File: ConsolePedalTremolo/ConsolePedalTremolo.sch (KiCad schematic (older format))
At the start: 30 parts, among them J1 Conn_02x25_Counter_Clockwise, Q1 BC550, Q2 BC550, Q3 BC550

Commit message: Assigned footprints. Need to add another resistor since the only ptv09 potentiometers I could find only went up to 500k
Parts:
- C1, C2, C3, C4, C6, C7: footprint (none) -> Capacitor_THT:C_Axial_L12.0mm_D6.5mm_P20.00mm_Horizontal
- C5: footprint (none) -> Capacitor_THT:CP_Axial_L11.0mm_D6.0mm_P18.00mm_Horizontal
- R1, R10, R11, R12, R13, R2, R4, R5, R6, R7, R8, R9: footprint (none) -> Resistor_THT:R_Axial_DIN0207_L6.3mm_D2.5mm_P10.16mm_Horizontal
- RV1, RV2: footprint (none) -> Potentiometer_THT:Potentiometer_Bourns_PTV09A-1_Single_Vertical
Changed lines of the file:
@@
 F 0 "R1" H 3020 2896 50  0000 L CNN
 F 1 "1M" H 3020 2805 50  0000 L CNN
-F 2 "" V 2880 2850 50  0001 C CNN
+F 2 "Resistor_THT:R_Axial_DIN0207_L6.3mm_D2.5mm_P10.16mm_Horizontal" V 2880 2850 50  0001 C CNN
 F 3 "~" H 2950 2850 50  0001 C CNN
 	1    2950 2850
@@
 F 0 "C1" V 3048 2700 50  0000 C CNN
 F 1 "0.1uF" V 3139 2700 50  0000 C CNN
-F 2 "" H 3338 2550 50  0001 C CNN
+F 2 "Capacitor_THT:C_Axial_L12.0mm_D6.5mm_P20.00mm_Horizontal" H 3338 2550 50  0001 C CNN
 F 3 "~" H 3300 2700 50  0001 C CNN
 	1    3300 2700
@@
 F 0 "R2" V 3393 2700 50  0000 C CNN
 F 1 "100K" V 3484 2700 50  0000 C CNN
-F 2 "" V 3530 2700 50  0001 C CNN
+F 2 "Resistor_THT:R_Axial_DIN0207_L6.3mm_D2.5mm_P10.16mm_Horizontal" V 3530 2700 50  0001 C CNN
 F 3 "~" H 3600 2700 50  0001 C CNN
 	1    3600 2700
@@
 F 0 "C2" V 3648 2450 50  0000 C CNN
 F 1 "0.1uF" V 3739 2450 50  0000 C CNN
-F 2 "" H 3938 2300 50  0001 C CNN
+F 2 "Capacitor_THT:C_Axial_L12.0mm_D6.5mm_P20.00mm_Horizontal" H 3938 2300 50  0001 C CNN
 F 3 "~" H 3900 2450 50  0001 C CNN
 	1    3900 2450
@@
 F 0 "R4" H 3820 2996 50  0000 L CNN
 F 1 "4.7K" H 3820 2905 50  0000 L CNN
-F 2 "" V 3680 2950 50  0001 C CNN
+F 2 "Resistor_THT:R_Axial_DIN0207_L6.3mm_D2.5mm_P10.16mm_Horizontal" V 3680 2950 50  0001 C CNN
 F 3 "~" H 3750 2950 50  0001 C CNN
 	1    3750 2950
@@
 F 0 "R6" V 4043 2100 50  0000 C CNN
 F 1 "330K" V 4134 2100 50  0000 C CNN
-F 2 "" V 4180 2100 50  0001 C CNN
+F 2 "Resistor_THT:R_Axial_DIN0207_L6.3mm_D2.5mm_P10.16mm_Horizontal" V 4180 2100 50  0001 C CNN
 F 3 "~" H 4250 2100 50  0001 C CNN
 	1    4250 2100
@@
 F 0 "R7" H 4520 1896 50  0000 L CNN
 F 1 "15K" H 4520 1805 50  0000 L CNN
-F 2 "" V 4380 1850 50  0001 C CNN
+F 2 "Resistor_THT:R_Axial_DIN0207_L6.3mm_D2.5mm_P10.16mm_Horizontal" V 4380 1850 50  0001 C CNN
 F 3 "~" H 4450 1850 50  0001 C CNN
 	1    4450 1850
@@
 F 0 "R8" H 4520 2846 50  0000 L CNN
 F 1 "15K" H 4520 2755 50  0000 L CNN
-F 2 "" V 4380 2800 50  0001 C CNN
+F 2 "Resistor_THT:R_Axial_DIN0207_L6.3mm_D2.5mm_P10.16mm_Horizontal" V 4380 2800 50  0001 C CNN
 F 3 "~" H 4450 2800 50  0001 C CNN
 	1    4450 2800
@@
 F 0 "R5" H 3820 3496 50  0000 L CNN
 F 1 "100K" H 3820 3405 50  0000 L CNN
-F 2 "" V 3680 3450 50  0001 C CNN
+F 2 "Resistor_THT:R_Axial_DIN0207_L6.3mm_D2.5mm_P10.16mm_Horizontal" V 3680 3450 50  0001 C CNN
 F 3 "~" H 3750 3450 50  0001 C CNN
 	1    3750 3450
@@
 F 0 "RV2" H 4930 3596 50  0000 R CNN
 F 1 "1M" H 4930 3505 50  0000 R CNN
-F 2 "" H 5000 3550 50  0001 C CNN
+F 2 "Potentiometer_THT:Potentiometer_Bourns_PTV09A-1_Single_Vertical" H 5000 3550 50  0001 C CNN
 F 3 "~" H 5000 3550 50  0001 C CNN
 	1    5000 3550
@@
 F 0 "C5" V 5705 3550 50  0000 C CNN
 F 1 "10uF" V 5614 3550 50  0000 C CNN
-F 2 "" H 5488 3400 50  0001 C CNN
+F 2 "Capacitor_THT:CP_Axial_L11.0mm_D6.0mm_P18.00mm_Horizontal" H 5488 3400 50  0001 C CNN
 F 3 "~" H 5450 3550 50  0001 C CNN
 	1    5450 3550
@@
 F 0 "C3" V 5052 2100 50  0000 C CNN
 F 1 "0.1uF" V 4961 2100 50  0000 C CNN
-F 2 "" H 4838 1950 50  0001 C CNN
+F 2 "Capacitor_THT:C_Axial_L12.0mm_D6.5mm_P20.00mm_Horizontal" H 4838 1950 50  0001 C CNN
 F 3 "~" H 4800 2100 50  0001 C CNN
 	1    4800 2100
@@
 F 0 "R12" H 5770 3446 50  0000 L CNN
 F 1 "100K" H 5770 3355 50  0000 L CNN
-F 2 "" V 5630 3400 50  0001 C CNN
+F 2 "Resistor_THT:R_Axial_DIN0207_L6.3mm_D2.5mm_P10.16mm_Horizontal" V 5630 3400 50  0001 C CNN
 F 3 "~" H 5700 3400 50  0001 C CNN
 	1    5700 3400
@@
 F 0 "R10" H 5370 2296 50  0000 L CNN
 F 1 "1M" H 5370 2205 50  0000 L CNN
-F 2 "" V 5230 2250 50  0001 C CNN
+F 2 "Resistor_THT:R_Axial_DIN0207_L6.3mm_D2.5mm_P10.16mm_Horizontal" V 5230 2250 50  0001 C CNN
 F 3 "~" H 5300 2250 50  0001 C CNN
 	1    5300 2250
@@
 F 0 "R11" V 5343 3950 50  0000 C CNN
 F 1 "3M" V 5434 3950 50  0000 C CNN
-F 2 "" V 5480 3950 50  0001 C CNN
+F 2 "Resistor_THT:R_Axial_DIN0207_L6.3mm_D2.5mm_P10.16mm_Horizontal" V 5480 3950 50  0001 C CNN
 F 3 "~" H 5550 3950 50  0001 C CNN
 	1    5550 3950
@@
 F 0 "C6" V 5798 3950 50  0000 C CNN
 F 1 "0.22uF" V 5889 3950 50  0000 C CNN
-F 2 "" H 6088 3800 50  0001 C CNN
+F 2 "Capacitor_THT:C_Axial_L12.0mm_D6.5mm_P20.00mm_Horizontal" H 6088 3800 50  0001 C CNN
 F 3 "~" H 6050 3950 50  0001 C CNN
 	1    6050 3950
@@
 F 0 "C7" V 6198 3950 50  0000 C CNN
 F 1 "0.22uF" V 6289 3950 50  0000 C CNN
-F 2 "" H 6488 3800 50  0001 C CNN
+F 2 "Capacitor_THT:C_Axial_L12.0mm_D6.5mm_P20.00mm_Horizontal" H 6488 3800 50  0001 C CNN
 F 3 "~" H 6450 3950 50  0001 C CNN
 	1    6450 3950
@@
 F 0 "R13" H 6320 4296 50  0000 L CNN
 F 1 "100K" H 6320 4205 50  0000 L CNN
-F 2 "" V 6180 4250 50  0001 C CNN
+F 2 "Resistor_THT:R_Axial_DIN0207_L6.3mm_D2.5mm_P10.16mm_Horizontal" V 6180 4250 50  0001 C CNN
 F 3 "~" H 6250 4250 50  0001 C CNN
 	1    6250 4250
@@
 F 0 "C4" V 4898 4250 50  0000 C CNN
 F 1 "0.22uF" V 4989 4250 50  0000 C CNN
-F 2 "" H 5188 4100 50  0001 C CNN
+F 2 "Capacitor_THT:C_Axial_L12.0mm_D6.5mm_P20.00mm_Horizontal" H 5188 4100 50  0001 C CNN
 F 3 "~" H 5150 4250 50  0001 C CNN
 	1    5150 4250
@@
 F 0 "R9" V 4543 4250 50  0000 C CNN
 F 1 "5.6K" V 4634 4250 50  0000 C CNN
-F 2 "" V 4680 4250 50  0001 C CNN
+F 2 "Resistor_THT:R_Axial_DIN0207_L6.3mm_D2.5mm_P10.16mm_Horizontal" V 4680 4250 50  0001 C CNN
 F 3 "~" H 4750 4250 50  0001 C CNN
 	1    4750 4250
@@
 F 0 "RV1" H 4331 4446 50  0000 R CNN
 F 1 "250K" H 4331 4355 50  0000 R CNN
-F 2 "" H 4400 4400 50  0001 C CNN
+F 2 "Potentiometer_THT:Potentiometer_Bourns_PTV09A-1_Single_Vertical" H 4400 4400 50  0001 C CNN
 F 3 "~" H 4400 4400 50  0001 C CNN
 	1    4400 4400

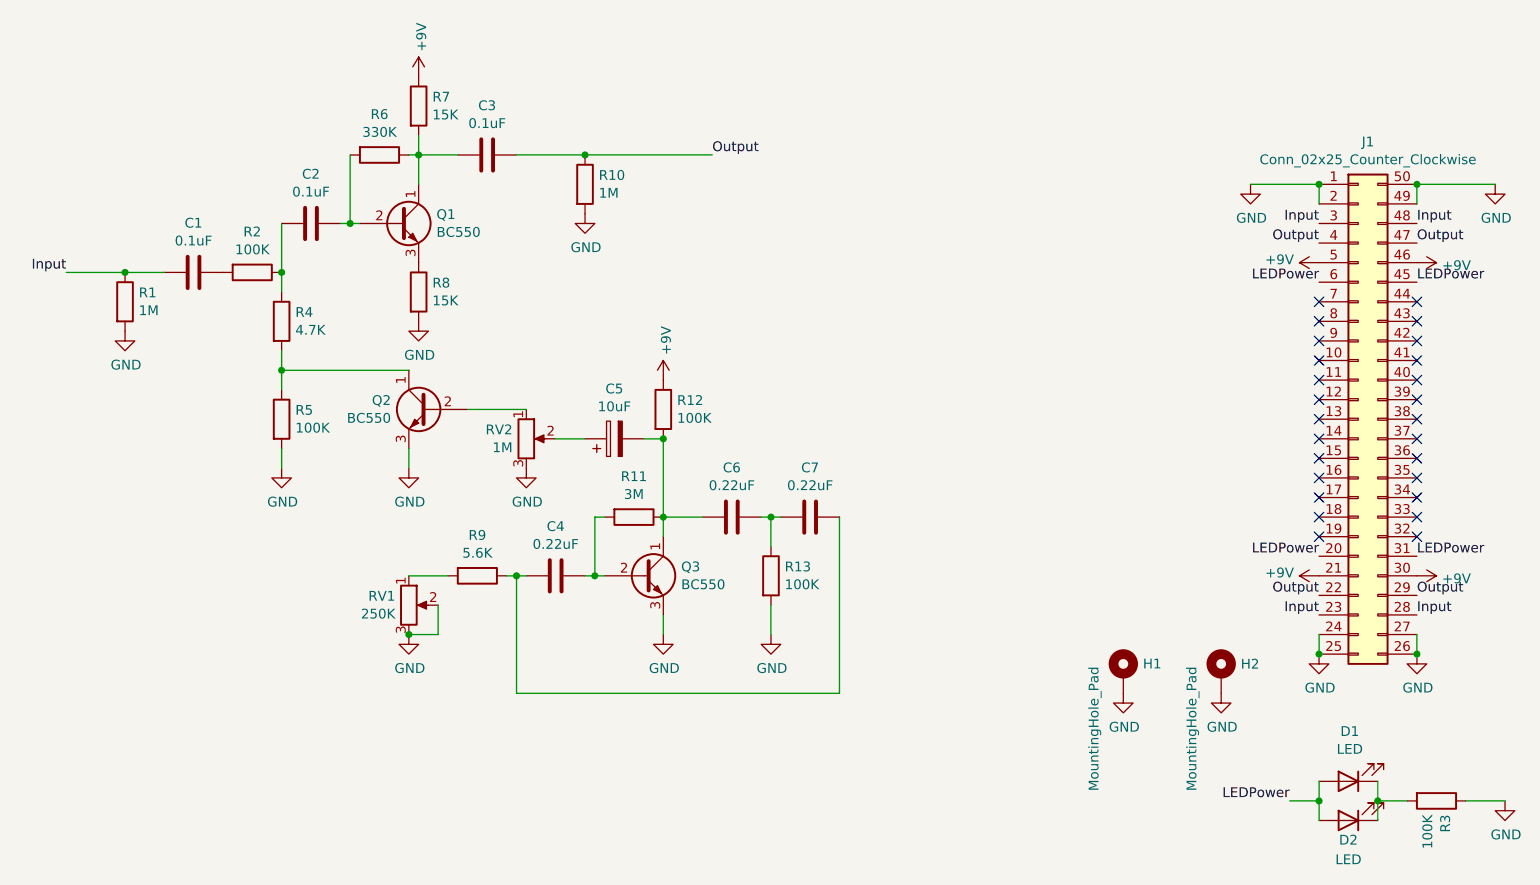
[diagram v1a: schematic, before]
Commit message: Added trimpots since I couldn't get the main potentiometers to the right resistance on their own.
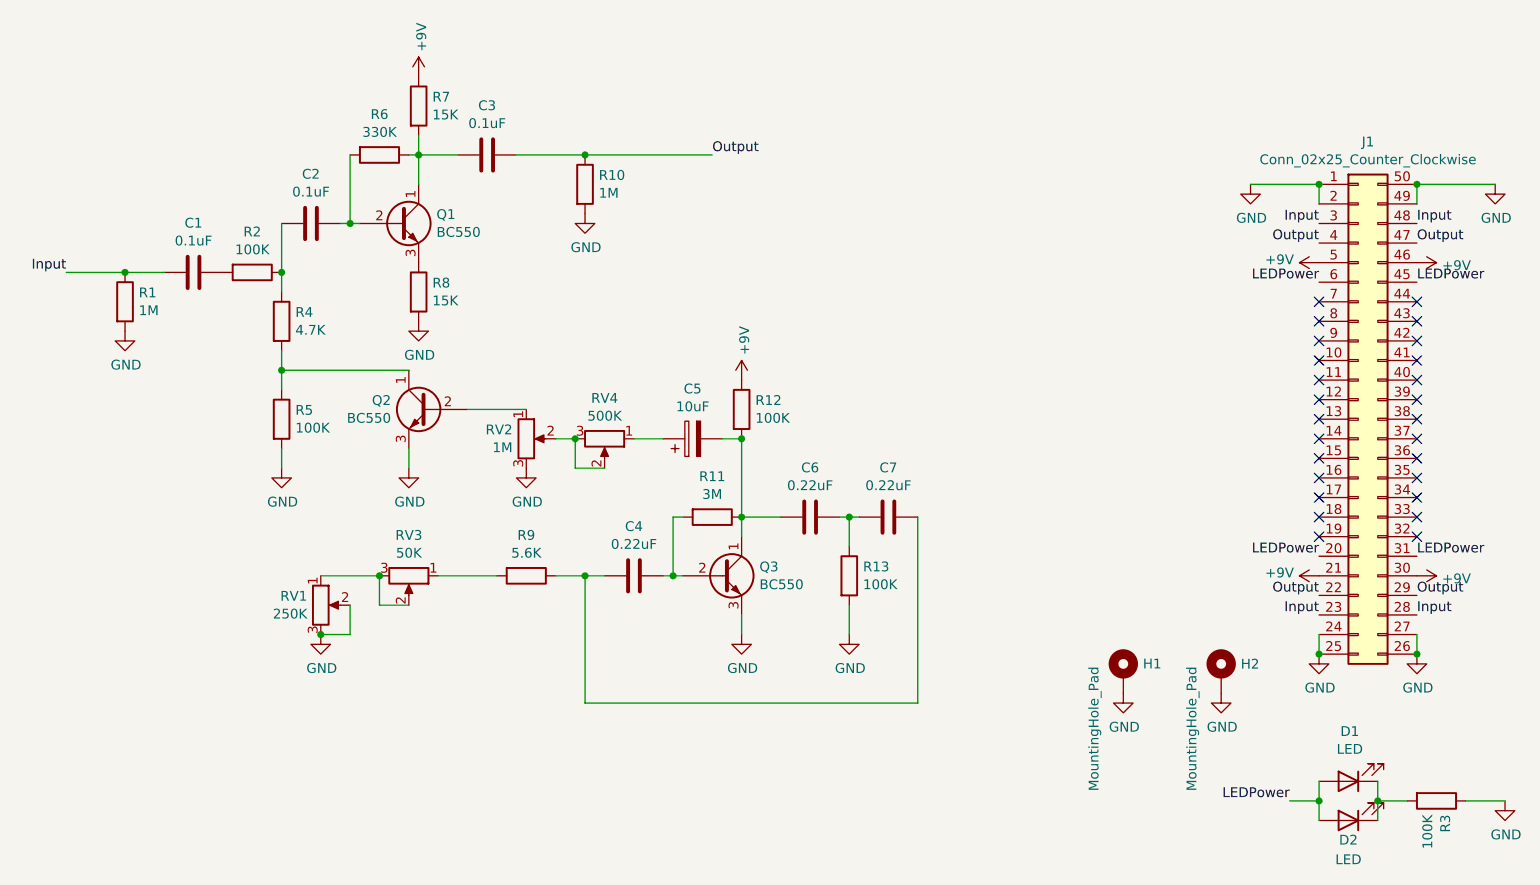
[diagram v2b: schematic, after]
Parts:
- added RV3: 50K, Potentiometer_THT:Potentiometer_Bourns_3386F_Vertical, symbol Device:R_POT
- added RV4: 500K, Potentiometer_THT:Potentiometer_Bourns_3386F_Vertical, symbol Device:R_POT
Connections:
- net at RV2.2: now also RV4.2, RV4.3; no longer C5.1
- net at R9.2: now also RV3.1; no longer RV1.1
- new net: C5.1, RV4.1
- new net: RV1.1, RV3.2, RV3.3
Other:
- moved on the sheet: C4, C5, C6, C7, Q3, R11, R12, R13, R9, RV1

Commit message: Created my own footprint for one of those square capacitors to lay flat since the axial ones are a little too much in diameter
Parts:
- C1, C2, C3, C4, C6, C7: footprint Capacitor_THT:C_Axial_L12.0mm_D6.5mm_P20.00mm_Horizontal -> libraries:C_Flat_L7.2_H6.5
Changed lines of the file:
@@
 F 0 "C1" V 3048 2700 50  0000 C CNN
 F 1 "0.1uF" V 3139 2700 50  0000 C CNN
-F 2 "Capacitor_THT:C_Axial_L12.0mm_D6.5mm_P20.00mm_Horizontal" H 3338 2550 50  0001 C CNN
+F 2 "libraries:C_Flat_L7.2_H6.5" H 3338 2550 50  0001 C CNN
 F 3 "~" H 3300 2700 50  0001 C CNN
 	1    3300 2700
@@
 F 0 "C2" V 3648 2450 50  0000 C CNN
 F 1 "0.1uF" V 3739 2450 50  0000 C CNN
-F 2 "Capacitor_THT:C_Axial_L12.0mm_D6.5mm_P20.00mm_Horizontal" H 3938 2300 50  0001 C CNN
+F 2 "libraries:C_Flat_L7.2_H6.5" H 3938 2300 50  0001 C CNN
 F 3 "~" H 3900 2450 50  0001 C CNN
 	1    3900 2450
@@
 F 0 "C3" V 5052 2100 50  0000 C CNN
 F 1 "0.1uF" V 4961 2100 50  0000 C CNN
-F 2 "Capacitor_THT:C_Axial_L12.0mm_D6.5mm_P20.00mm_Horizontal" H 4838 1950 50  0001 C CNN
+F 2 "libraries:C_Flat_L7.2_H6.5" H 4838 1950 50  0001 C CNN
 F 3 "~" H 4800 2100 50  0001 C CNN
 	1    4800 2100
@@
 F 0 "C6" V 6198 3950 50  0000 C CNN
 F 1 "0.22uF" V 6289 3950 50  0000 C CNN
-F 2 "Capacitor_THT:C_Axial_L12.0mm_D6.5mm_P20.00mm_Horizontal" H 6488 3800 50  0001 C CNN
+F 2 "libraries:C_Flat_L7.2_H6.5" H 6488 3800 50  0001 C CNN
 F 3 "~" H 6450 3950 50  0001 C CNN
 	1    6450 3950
@@
 F 0 "C7" V 6598 3950 50  0000 C CNN
 F 1 "0.22uF" V 6689 3950 50  0000 C CNN
-F 2 "Capacitor_THT:C_Axial_L12.0mm_D6.5mm_P20.00mm_Horizontal" H 6888 3800 50  0001 C CNN
+F 2 "libraries:C_Flat_L7.2_H6.5" H 6888 3800 50  0001 C CNN
 F 3 "~" H 6850 3950 50  0001 C CNN
 	1    6850 3950
@@
 F 0 "C4" V 5298 4250 50  0000 C CNN
 F 1 "0.22uF" V 5389 4250 50  0000 C CNN
-F 2 "Capacitor_THT:C_Axial_L12.0mm_D6.5mm_P20.00mm_Horizontal" H 5588 4100 50  0001 C CNN
+F 2 "libraries:C_Flat_L7.2_H6.5" H 5588 4100 50  0001 C CNN
 F 3 "~" H 5550 4250 50  0001 C CNN
 	1    5550 4250

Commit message: Added new pcb project
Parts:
- R8: value 15K -> 1.5K
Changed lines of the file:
@@
 P 4450 2800
 F 0 "R8" H 4520 2846 50  0000 L CNN
-F 1 "15K" H 4520 2755 50  0000 L CNN
+F 1 "1.5K" H 4520 2755 50  0000 L CNN
 F 2 "Resistor_THT:R_Axial_DIN0207_L6.3mm_D2.5mm_P10.16mm_Horizontal" V 4380 2800 50  0001 C CNN
 F 3 "~" H 4450 2800 50  0001 C CNN
